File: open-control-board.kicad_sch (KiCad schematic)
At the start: 187 parts, among them CN1 LCC Port, CN14 Conn_02x06_Odd_Even, CN2 Conn_01x06_Pin, CN3 12V Separate Supply, CN4 Conn_02x05_Counter_Clockwise, CN5 NTC Brew Boiler, CN6 NTC Service Boiler, CN7 Conn_01x06_Pin, CN8 Conn_01x05_Pin, CN9 Conn_02x04, J1 USB_B_Micro, J13 Conn_02x05_Odd_Even, J15 Conn_02x05_Odd_Even, J16 USB_B_Micro, J3 Conn_02x03_Odd_Even, J4 Molex_0525591853, J5 BM04B-SRSS-TB(LF)(SN), J5 Micro_SD_Card_Det_Hirose_DM3AT, Q1 DMP21D0UT-7, Q10 DMG1012T-7, Q11 DMN63D8LDW, Q12 DMN63D8LDW, Q13 DMG1012T-7, Q14 DMG1012T-7, Q15 DMP21D0UT-7, Q2 DMP21D0UT-7, Q3 Q_PMOS-E_DUAL_Generic_SEP_S1G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, Q4 DMN63D8LDW, Q5 Q_PMOS-E_DUAL_Generic_SEP_S1G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, Q6 DMN63D8LDW, Q7 DMN63D8LDW, Q8 DMP21D0UT-7, Q9 DMG1012T-7, SW1 SW_Push, SW2 SW_Push, SW3 SW_Push, SW4 SW_Push, U10 FDC1004, U11 TC2014-5.0VxCTTR, U15 STPIC6C595TTR, U16 STPIC6C595TTR, U2 RP2040, U3 ESP32-S3-WROOM-1, U4 W25Q16JVUXIQ, U6 ADS124S08IPBSR, U6 TPS82130, U7 LM5050-1, U8 LM5050-1, Y1 XYDBPCNANF-12MHZ

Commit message: Re-added LED and fixed silk screen
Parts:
- added D4: KT-0603W, LED_SMD:LED_0603_1608Metric, symbol Device:LED
- added Q16: DMG1012T-7, Package_TO_SOT_SMD:SOT-523, symbol Transistor_FET:ZXMN2B14FH
- added R12: 120R, Resistor_SMD:R_0402_1005Metric, symbol Device:R_Small
- C39, C42: footprint Resistor_SMD:R_0805_2012Metric_Pad1.20x1.40mm_HandSolder -> Capacitor_SMD:C_0805_2012Metric_Pad1.18x1.45mm_HandSolder; now left out of the parts list
- C48: value C_Small -> 6.8 nF, 50V; LCSC (none) -> C1542
- CN5, CN6, JP1, JP10, JP13, JP17, JP2, JP20, JP21, JP22, JP23, JP3, JP7, R4, R66: now left out of the parts list
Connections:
- net +3V3: now also R12.1
- net CN14_10: now also Q16.1 (G)
- net GND: now also Q16.2 (S)
- new net: D4.1 (K), Q16.3 (D)
- new net: D4.2 (A), R12.2

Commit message: Updated capacitor footprint
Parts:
- C39, C42: footprint Capacitor_SMD:C_0805_2012Metric_Pad1.18x1.45mm_HandSolder -> Capacitor_SMD:C_1206_3216Metric_Pad1.33x1.80mm_HandSolder
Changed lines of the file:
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@@
       (effects (font (size 1.27 1.27)) (justify right))
     )
-    (property "Footprint" "Capacitor_SMD:C_0805_2012Metric_Pad1.18x1.45mm_HandSolder" (at 72.39 661.67 0)
+    (property "Footprint" "Capacitor_SMD:C_1206_3216Metric_Pad1.33x1.80mm_HandSolder" (at 72.39 661.67 0)
       (effects (font (size 1.27 1.27)) hide)
     )
@@
       (effects (font (size 1.27 1.27)) (justify right))
     )
-    (property "Footprint" "Capacitor_SMD:C_0805_2012Metric_Pad1.18x1.45mm_HandSolder" (at 72.39 618.49 0)
-      (effects (font (size 1.27 1.27)) hide)
-    )
+    (property "Footprint" "Capacitor_SMD:C_1206_3216Metric_Pad1.33x1.80mm_HandSolder" (at 72.39 618.49 0)
+      (effects (font (size 1.27 1.27)) hide)
+    )

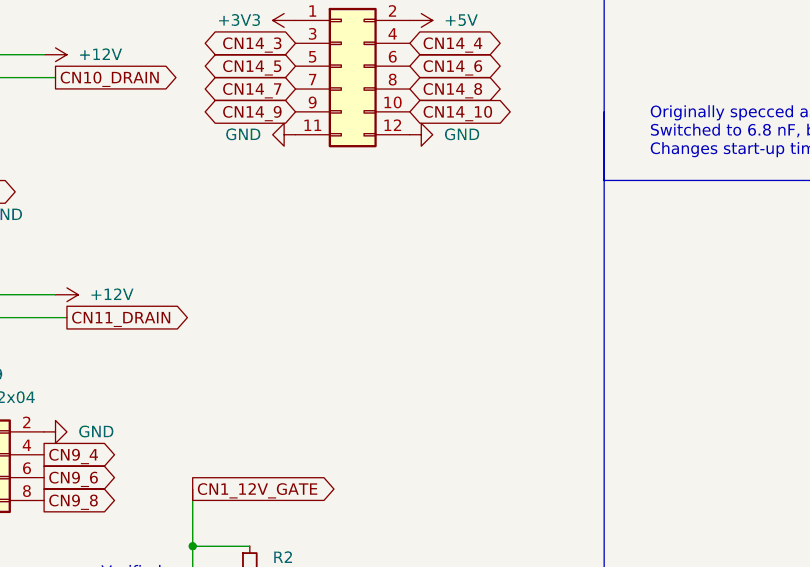
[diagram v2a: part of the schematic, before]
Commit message: Added more power connectors to CN9
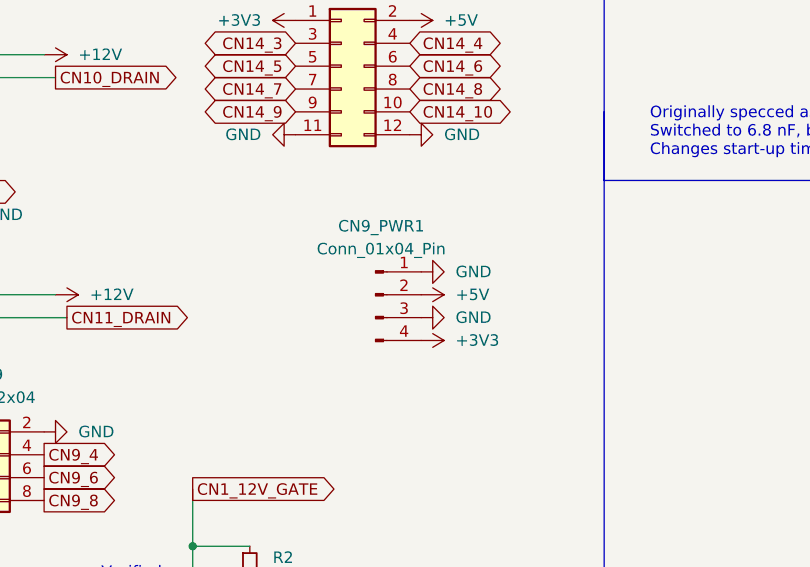
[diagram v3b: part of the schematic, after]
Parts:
- added CN9_PWR1: Conn_01x04_Pin, Connector_PinHeader_2.54mm:PinHeader_1x04_P2.54mm_Vertical, symbol Connector:Conn_01x04_Pin
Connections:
- net +3V3: now also CN9_PWR1.4 (Pin_4)
- net +5V: now also CN9_PWR1.2 (Pin_2)
- net GND: now also CN9_PWR1.1 (Pin_1), CN9_PWR1.3 (Pin_3)
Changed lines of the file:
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@@
     )
   )
+  (symbol (lib_id "power:GND") (at 83.82 128.27 90) (unit 1)
+    (in_bom yes) (on_board yes) (dnp no) (fields_autoplaced)
+    (property "Reference" "#PWR0174" (at 90.17 128.27 0)
+      (effects (font (size 1.27 1.27)) hide)
+    )
+    (property "Value" "GND" (at 87.63 128.27 90)
+      (effects (font (size 1.27 1.27)) (justify right))
+    )
+    (property "Footprint" "" (at 83.82 128.27 0)
+      (effects (font (size 1.27 1.27)) hide)
+    )
+    (property "Datasheet" "" (at 83.82 128.27 0)
+      (effects (font (size 1.27 1.27)) hide)
+    )
+    (pin "1")
+    (instances
+      (project "open-control-board"
+        (path "/c7c8c763-88fa-419b-8f4a-ebade330cc39"
+          (reference "#PWR0174") (unit 1)
+        )
+      )
+    )
+  )
   (symbol (lib_id "Device:C_Small") (at 568.96 176.53 0) (unit 1)
     (in_bom no) (on_board yes) (dnp yes) (fields_autoplaced)
@@
     )
   )
+  (symbol (lib_id "power:+5V") (at 83.82 130.81 270) (unit 1)
+    (in_bom yes) (on_board yes) (dnp no) (fields_autoplaced)
+    (property "Reference" "#PWR0178" (at 80.01 130.81 0)
+      (effects (font (size 1.27 1.27)) hide)
+    )
+    (property "Value" "+5V" (at 87.63 130.81 90)
+      (effects (font (size 1.27 1.27)) (justify left))
+    )
+    (property "Footprint" "" (at 83.82 130.81 0)
+      (effects (font (size 1.27 1.27)) hide)
+    )
+    (property "Datasheet" "" (at 83.82 130.81 0)
+      (effects (font (size 1.27 1.27)) hide)
+    )
+    (pin "1")
+    (instances
+      (project "open-control-board"
+        (path "/c7c8c763-88fa-419b-8f4a-ebade330cc39"
+          (reference "#PWR0178") (unit 1)
+        )
+      )
+    )
+  )
   (symbol (lib_id "power:GND") (at 745.49 350.52 270) (unit 1)
     (in_bom yes) (on_board yes) (dnp no) (fields_autoplaced)
@@
     )
   )
+  (symbol (lib_id "Connector:Conn_01x04_Pin") (at 78.74 130.81 0) (unit 1)
+    (in_bom yes) (on_board yes) (dnp no) (fields_autoplaced)
+    (property "Reference" "CN9_PWR1" (at 79.375 123.19 0)
+      (effects (font (size 1.27 1.27)))
+    )
+    (property "Value" "Conn_01x04_Pin" (at 79.375 125.73 0)
+      (effects (font (size 1.27 1.27)))
+    )
+    (property "Footprint" "Connector_PinHeader_2.54mm:PinHeader_1x04_P2.54mm_Vertical" (at 78.74 130.81 0)
+      (effects (font (size 1.27 1.27)) hide)
+    )
+    (property "Datasheet" "~" (at 78.74 130.81 0)
+      (effects (font (size 1.27 1.27)) hide)
+    )
+    (pin "1")
+    (pin "2")
+    (pin "3")
+    (pin "4")
+    (instances
+      (project "open-control-board"
+        (path "/c7c8c763-88fa-419b-8f4a-ebade330cc39"
+          (reference "CN9_PWR1") (unit 1)
+        )
+      )
+    )
+  )
   (symbol (lib_id "Connector:Conn_01x02_Pin") (at 26.67 130.81 0) (unit 1)
     (in_bom no) (on_board yes) (dnp no) (fields_autoplaced)
@@
     )
   )
+  (symbol (lib_id "power:GND") (at 83.82 133.35 90) (unit 1)
+    (in_bom yes) (on_board yes) (dnp no) (fields_autoplaced)
+    (property "Reference" "#PWR0175" (at 90.17 133.35 0)
+      (effects (font (size 1.27 1.27)) hide)
+    )
+    (property "Value" "GND" (at 87.63 133.35 90)
+      (effects (font (size 1.27 1.27)) (justify right))
+    )
+    (property "Footprint" "" (at 83.82 133.35 0)
+      (effects (font (size 1.27 1.27)) hide)
+    )
+    (property "Datasheet" "" (at 83.82 133.35 0)
+      (effects (font (size 1.27 1.27)) hide)
+    )
+    (pin "1")
+    (instances
+      (project "open-control-board"
+        (path "/c7c8c763-88fa-419b-8f4a-ebade330cc39"
+          (reference "#PWR0175") (unit 1)
+        )
+      )
+    )
+  )
   (symbol (lib_id "power:GND") (at 224.79 34.29 270) (unit 1)
     (in_bom yes) (on_board yes) (dnp no) (fields_autoplaced)
@@
         )
       )
+    )
+  )
+  (symbol (lib_id "power:+3V3") (at 83.82 135.89 270) (unit 1)
+    (in_bom yes) (on_board yes) (dnp no) (fields_autoplaced)
+    (property "Reference" "#PWR0179" (at 80.01 135.89 0)
+      (effects (font (size 1.27 1.27)) hide)
+    )
+    (property "Value" "+3V3" (at 87.63 135.89 90)
+      (effects (font (size 1.27 1.27)) (justify left))
+    )
+    (property "Footprint" "" (at 83.82 135.89 0)
+      (effects (font (size 1.27 1.27)) hide)
+    )
+    (property "Datasheet" "" (at 83.82 135.89 0)
+      (effects (font (size 1.27 1.27)) hide)
+    )
+    (pin "1")
+    (instances
+      (project "open-control-board"
+        (path "/c7c8c763-88fa-419b-8f4a-ebade330cc39"
+          (reference "#PWR0179") (unit 1)
+        )
+      )

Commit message: Cleaned up schematic
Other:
- note added: "ESP32-S3 control of RP2040"
- note added: "ESP32-S3-WROOM-1U"
- note added: "EyeSPI Connector"
- note added: "RP2040 Debug (optional)"
- note added: "SD Card Reader (Optional)"
- note removed: "3V3 <-> 5V Bidirectional Level Shifter"
- note removed: "ADS1119 ADCs"
- note removed: "ESP32-S3-WROOM-1U (Optional)"
- note removed: "RP2040 Debug and Flash (optional)"
- moved on the sheet: C12, C24, C26, C28, C29, C3, C35, C36, C37, C38, C39, C40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

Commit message: Added some additional bypass caps for good measure
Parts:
- added C51: 1 uF, >6.3V, X5R, Capacitor_SMD:C_0201_0603Metric, symbol Device:C_Small
- added C52: 47 uF, Capacitor_SMD:C_1206_3216Metric_Pad1.33x1.80mm_HandSolder, symbol Device:C_Small
- added C53, C54: 100 nF, >10V, X6S, Capacitor_SMD:C_0201_0603Metric, symbol Device:C_Small
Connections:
- net +3V3: now also C52.1
- net +5V: now also C51.1, C53.2, C54.2
- net GND: now also C51.2, C52.2, C53.1, C54.1
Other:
- moved on the sheet: J5

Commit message: WIP
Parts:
- removed CN9: Conn_02x04, Connector_PinHeader_2.54mm:PinHeader_2x04_P2.54mm_Vertical, symbol Connector_Generic:Conn_02x04_Odd_Even
- removed CN9_PWR1: Conn_01x04_Pin, Connector_PinHeader_2.54mm:PinHeader_1x04_P2.54mm_Vertical, symbol Connector:Conn_01x04_Pin
- added CN9: ~, HugeConnector:Conn_3x04, symbol HugeConnector:Conn_3x04
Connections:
- net +12V: now also CN9.1
- net +3V3: now also CN9.9
- net +5V: now also CN9.11
- net CN9_3: now also CN9.3
- net CN9_4: now also CN9.4
- net CN9_5: now also CN9.5
- net CN9_6: now also CN9.6
- net CN9_7: now also CN9.7
- net CN9_8: now also CN9.8
- net GND: now also CN9.10, CN9.12, CN9.2

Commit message: Final updates (as sent to manufacturer)
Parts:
- added R45, R46, R47, R48, R49: 47R, Resistor_SMD:R_0201_0603Metric, symbol Device:R_Small
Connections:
- net ADC_CS: now also R49.2; no longer U6.9 (CS_N)
- net ADC_DRDY: now also R45.2; no longer U6.13 (DRDY_N)
- net INT_SPI_MISO: now also R46.2; no longer U6.12 (DOUT_DRDY_N)
- net INT_SPI_MOSI: now also R48.2; no longer U6.10 (DIN)
- net INT_SPI_SCLK: now also R47.2; no longer U6.11 (SCLK)
- new net: R48.1, U6.10 (DIN)
- new net: R47.1, U6.11 (SCLK)
- new net: R46.1, U6.12 (DOUT_DRDY_N)
- new net: R45.1, U6.13 (DRDY_N)
- new net: R49.1, U6.9 (CS_N)
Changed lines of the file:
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@@
     (stroke (width 0) (type default))
   )
+  (wire (pts (xy 918.21 69.85) (xy 910.59 69.85))
+    (stroke (width 0) (type default))
+  )
   (wire (pts (xy 486.41 49.53) (xy 494.03 49.53))
     (stroke (width 0) (type default))
@@
     (stroke (width 0) (type default))
   )
+  (wire (pts (xy 918.21 64.77) (xy 910.59 64.77))
+    (stroke (width 0) (type default))
+  )
   (wire (pts (xy 363.22 167.64) (xy 353.06 167.64))
     (stroke (width 0) (type default))
@@
     (stroke (width 0) (type default))
   )
+  (wire (pts (xy 918.21 74.93) (xy 910.59 74.93))
+    (stroke (width 0) (type default))
+  )
   (wire (pts (xy 934.72 227.33) (xy 941.07 227.33))
     (stroke (width 0) (type default))
@@
     (stroke (width 0) (type default))
   )
+  (wire (pts (xy 905.51 69.85) (xy 899.16 69.85))
+    (stroke (width 0) (type default))
+  )
   (wire (pts (xy 330.2 67.31) (xy 330.2 106.68))
     (stroke (width 0) (type default))
@@
     (stroke (width 0) (type default))
   )
+  (wire (pts (xy 905.51 64.77) (xy 899.16 64.77))
+    (stroke (width 0) (type default))
+  )
   (wire (pts (xy 64.77 289.56) (xy 72.39 289.56))
     (stroke (width 0) (type default))
@@
     (stroke (width 0) (type default))
   )
+  (wire (pts (xy 905.51 85.09) (xy 899.16 85.09))
+    (stroke (width 0) (type default))
+  )
   (wire (pts (xy 835.66 101.6) (xy 835.66 105.41))
     (stroke (width 0) (type default))
@@
     (stroke (width 0) (type default))
   )
+  (wire (pts (xy 905.51 80.01) (xy 899.16 80.01))
+    (stroke (width 0) (type default))
+  )
   (polyline (pts (xy 12.7 379.73) (xy 104.14 379.73))
     (stroke (width 0) (type default))
@@
     (stroke (width 0) (type default))
   )
+  (wire (pts (xy 905.51 74.93) (xy 899.16 74.93))
+    (stroke (width 0) (type default))
+  )
   (wire (pts (xy 148.59 312.42) (xy 151.13 312.42))
     (stroke (width 0) (type default))
@@
     (stroke (width 0) (type default))
   )
+  (wire (pts (xy 918.21 80.01) (xy 910.59 80.01))
+    (stroke (width 0) (type default))
+  )
   (wire (pts (xy 511.81 373.38) (xy 525.78 373.38))
     (stroke (width 0) (type default))
@@
     (stroke (width 0) (type default))
   )
+  (wire (pts (xy 918.21 85.09) (xy 910.59 85.09))
+    (stroke (width 0) (type default))
+  )
   (wire (pts (xy 88.9 487.68) (xy 88.9 492.76))
     (stroke (width 0) (type default))
@@
     )
   )
-  (global_label "INT_SPI_SCLK" (shape input) (at 899.16 74.93 0) (fields_autoplaced)
+  (global_label "INT_SPI_SCLK" (shape input) (at 918.21 74.93 0) (fields_autoplaced)
     (effects (font (size 1.27 1.27)) (justify left))
-    (property "Intersheetrefs" "${INTERSHEET_REFS}" (at 914.8452 74.93 0)
+    (property "Intersheetrefs" "${INTERSHEET_REFS}" (at 933.8952 74.93 0)
       (effects (font (size 1.27 1.27)) (justify left) hide)
     )
@@
     )
   )
-  (global_label "INT_SPI_MISO" (shape output) (at 899.16 69.85 0) (fields_autoplaced)
+  (global_label "INT_SPI_MISO" (shape output) (at 918.21 69.85 0) (fields_autoplaced)
     (effects (font (size 1.27 1.27)) (justify left))
-    (property "Intersheetrefs" "${INTERSHEET_REFS}" (at 914.6638 69.85 0)
+    (property "Intersheetrefs" "${INTERSHEET_REFS}" (at 933.7138 69.85 0)
       (effects (font (size 1.27 1.27)) (justify left) hide)
     )
@@
     )
   )
-  (global_label "ADC_CS" (shape input) (at 899.16 85.09 0) (fields_autoplaced)
+  (global_label "ADC_CS" (shape input) (at 918.21 85.09 0) (fields_autoplaced)
     (effects (font (size 1.27 1.27)) (justify left))
-    (property "Intersheetrefs" "${INTERSHEET_REFS}" (at 909.2209 85.09 0)
+    (property "Intersheetrefs" "${INTERSHEET_REFS}" (at 928.2709 85.09 0)
       (effects (font (size 1.27 1.27)) (justify left) hide)
     )
@@
     )
   )
-  (global_label "ADC_DRDY" (shape output) (at 899.16 64.77 0) (fields_autoplaced)
+  (global_label "ADC_DRDY" (shape output) (at 918.21 64.77 0) (fields_autoplaced)
     (effects (font (size 1.27 1.27)) (justify left))
-    (property "Intersheetrefs" "${INTERSHEET_REFS}" (at 911.64 64.77 0)
+    (property "Intersheetrefs" "${INTERSHEET_REFS}" (at 930.69 64.77 0)
       (effects (font (size 1.27 1.27)) (justify left) hide)
     )
@@
     )
   )
-  (global_label "INT_SPI_MOSI" (shape input) (at 899.16 80.01 0) (fields_autoplaced)
+  (global_label "INT_SPI_MOSI" (shape input) (at 918.21 80.01 0) (fields_autoplaced)
     (effects (font (size 1.27 1.27)) (justify left))
-    (property "Intersheetrefs" "${INTERSHEET_REFS}" (at 914.6638 80.01 0)
+    (property "Intersheetrefs" "${INTERSHEET_REFS}" (at 933.7138 80.01 0)
       (effects (font (size 1.27 1.27)) (justify left) hide)
     )
@@
     )
   )
+  (symbol (lib_id "Device:R_Small") (at 908.05 69.85 90) (unit 1)
+    (in_bom yes) (on_board yes) (dnp no) (fields_autoplaced)
+    (property "Reference" "R46" (at 908.05 64.77 90)
+      (effects (font (size 1.27 1.27)))
+    )
+    (property "Value" "47R" (at 908.05 67.31 90)
+      (effects (font (size 1.27 1.27)))
+    )
+    (property "Footprint" "Resistor_SMD:R_0201_0603Metric" (at 908.05 69.85 0)
+      (effects (font (size 1.27 1.27)) hide)
+    )
+    (property "Datasheet" "~" (at 908.05 69.85 0)
+      (effects (font (size 1.27 1.27)) hide)
+    )
+    (property "LCSC" "C273279" (at 908.05 69.85 0)
+      (effects (font (size 1.27 1.27)) hide)
+    )
+    (pin "1")
+    (pin "2")
+    (instances
+      (project "open-control-board"
+        (path "/c7c8c763-88fa-419b-8f4a-ebade330cc39"
+          (reference "R46") (unit 1)
+        )
+      )
+    )
+  )
   (symbol (lib_id "power:+3V3") (at 659.13 189.23 180) (unit 1)
     (in_bom yes) (on_board yes) (dnp no) (fields_autoplaced)
@@
     )
   )
+  (symbol (lib_id "Device:R_Small") (at 908.05 64.77 90) (unit 1)
+    (in_bom yes) (on_board yes) (dnp no) (fields_autoplaced)
+    (property "Reference" "R45" (at 908.05 59.69 90)
+      (effects (font (size 1.27 1.27)))
+    )
+    (property "Value" "47R" (at 908.05 62.23 90)
+      (effects (font (size 1.27 1.27)))
+    )
+    (property "Footprint" "Resistor_SMD:R_0201_0603Metric" (at 908.05 64.77 0)
+      (effects (font (size 1.27 1.27)) hide)
+    )
+    (property "Datasheet" "~" (at 908.05 64.77 0)
+      (effects (font (size 1.27 1.27)) hide)
+    )
+    (property "LCSC" "C273279" (at 908.05 64.77 0)
+      (effects (font (size 1.27 1.27)) hide)
+    )
+    (pin "1")
+    (pin "2")
+    (instances
+      (project "open-control-board"
+        (path "/c7c8c763-88fa-419b-8f4a-ebade330cc39"
+          (reference "R45") (unit 1)
+        )
+      )
+    )
+  )
   (symbol (lib_id "TPIC6C595:TPIC6C595DG4") (at 170.18 215.9 0) (unit 1)
     (in_bom yes) (on_board yes) (dnp no) (fields_autoplaced)
@@
     )
   )
+  (symbol (lib_id "Device:R_Small") (at 908.05 74.93 90) (unit 1)
+    (in_bom yes) (on_board yes) (dnp no) (fields_autoplaced)
+    (property "Reference" "R47" (at 908.05 69.85 90)
+      (effects (font (size 1.27 1.27)))
+    )
+    (property "Value" "47R" (at 908.05 72.39 90)
+      (effects (font (size 1.27 1.27)))
+    )
+    (property "Footprint" "Resistor_SMD:R_0201_0603Metric" (at 908.05 74.93 0)
+      (effects (font (size 1.27 1.27)) hide)
+    )
+    (property "Datasheet" "~" (at 908.05 74.93 0)
+      (effects (font (size 1.27 1.27)) hide)
+    )
+    (property "LCSC" "C273279" (at 908.05 74.93 0)
+      (effects (font (size 1.27 1.27)) hide)
+    )
+    (pin "1")
+    (pin "2")
+    (instances
+      (project "open-control-board"
+        (path "/c7c8c763-88fa-419b-8f4a-ebade330cc39"
+          (reference "R47") (unit 1)
+        )
+      )
+    )
+  )
   (symbol (lib_id "power:GND") (at 134.62 102.87 0) (unit 1)
     (in_bom yes) (on_board yes) (dnp no)
@@
     )
   )
+  (symbol (lib_id "Device:R_Small") (at 908.05 80.01 90) (unit 1)
+    (in_bom yes) (on_board yes) (dnp no) (fields_autoplaced)
+    (property "Reference" "R48" (at 908.05 74.93 90)
+      (effects (font (size 1.27 1.27)))
+    )
+    (property "Value" "47R" (at 908.05 77.47 90)
+      (effects (font (size 1.27 1.27)))
+    )
+    (property "Footprint" "Resistor_SMD:R_0201_0603Metric" (at 908.05 80.01 0)
+      (effects (font (size 1.27 1.27)) hide)
+    )
+    (property "Datasheet" "~" (at 908.05 80.01 0)
+      (effects (font (size 1.27 1.27)) hide)
+    )
+    (property "LCSC" "C273279" (at 908.05 80.01 0)
+      (effects (font (size 1.27 1.27)) hide)
+    )
+    (pin "1")
+    (pin "2")
+    (instances
+      (project "open-control-board"
+        (path "/c7c8c763-88fa-419b-8f4a-ebade330cc39"
+          (reference "R48") (unit 1)
+        )
+      )
+    )
+  )
   (symbol (lib_id "Device:C_Small") (at 134.62 40.64 0) (unit 1)
     (in_bom yes) (on_board yes) (dnp no)
@@
         )
       )
+    )
+  )
+  (symbol (lib_id "Device:R_Small") (at 908.05 85.09 90) (unit 1)
+    (in_bom yes) (on_board yes) (dnp no) (fields_autoplaced)
+    (property "Reference" "R49" (at 908.05 80.01 90)
+      (effects (font (size 1.27 1.27)))
+    )
+    (property "Value" "47R" (at 908.05 82.55 90)
+      (effects (font (size 1.27 1.27)))
+    )
+    (property "Footprint" "Resistor_SMD:R_0201_0603Metric" (at 908.05 85.09 0)
+      (effects (font (size 1.27 1.27)) hide)
+    )
+    (property "Datasheet" "~" (at 908.05 85.09 0)
+      (effects (font (size 1.27 1.27)) hide)
+    )
+    (property "LCSC" "C273279" (at 908.05 85.09 0)
+      (effects (font (size 1.27 1.27)) hide)
+    )
+    (pin "1")
+    (pin "2")
+    (instances
+      (project "open-control-board"
+        (path "/c7c8c763-88fa-419b-8f4a-ebade330cc39"
+          (reference "R49") (unit 1)
+        )
+      )
